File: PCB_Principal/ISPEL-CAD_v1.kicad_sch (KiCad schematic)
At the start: 21 parts, among them J1 Vin, J10 E1, J11 S1, J12 E2, J13 S2, J14 FRENTE, J15 PRUEBA_5V, J2 GND_NUCLEO, J3 CN8_NUCLEO, J4 CN9_NUCLEO, J5 GND_NUCLEO, J6 GND_NUCLEO, J7 CN7_NUCLEO, J8 CN10_NUCLEO, J9 GND_NUCLEO

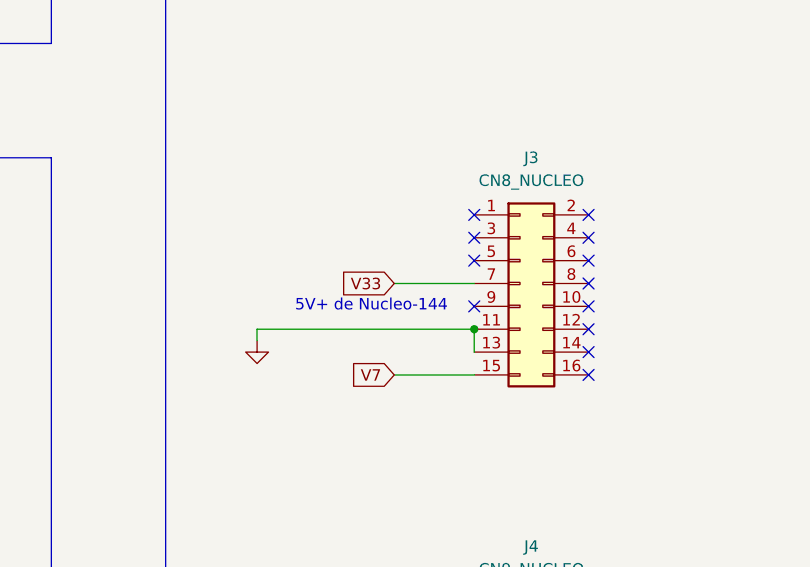
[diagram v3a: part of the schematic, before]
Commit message: Placa PCB con ERC. Falta huella de portafusibles.
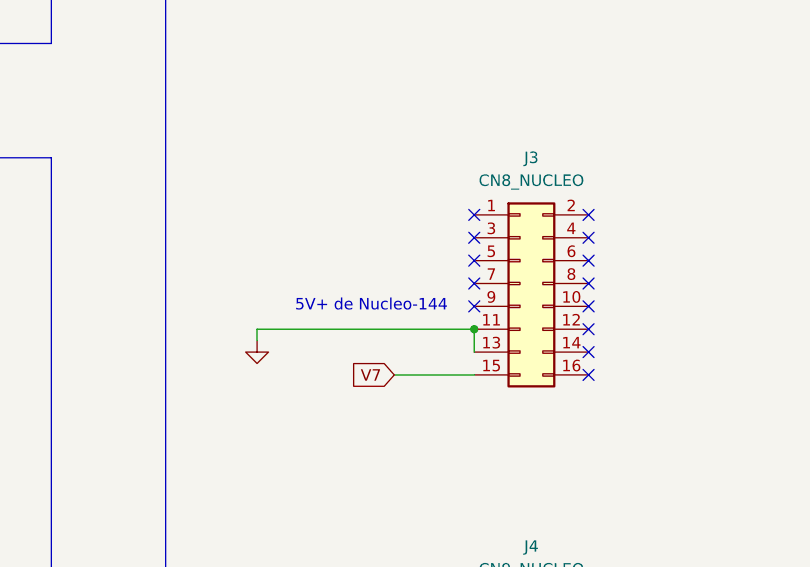
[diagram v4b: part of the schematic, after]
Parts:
- J3: footprint Connector_PinSocket_2.54mm:PinSocket_2x08_P2.54mm_Vertical -> Libreria_ISPEL:PinSocket_2x08_P2.54mm_Vertical_impar-par
- J4: footprint Connector_PinSocket_2.54mm:PinSocket_2x16_P2.54mm_Vertical -> Libreria_ISPEL:PinSocket_2x16_P2.54mm_Vertical_impar-par
- J7: footprint Connector_PinSocket_2.54mm:PinSocket_2x10_P2.54mm_Vertical -> Libreria_ISPEL:PinSocket_2x10_P2.54mm_Vertical_impar-par
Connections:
- net V33: no longer names the net of J3.7 (Pin_7)
- no-connect marks 61 -> 62
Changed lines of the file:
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@@
 	)
 	(no_connect
+		(at 110.49 153.67)
+	)
+	(no_connect
 		(at 186.69 163.83)
 	)
@@
 	(wire
 		(pts
-			(xy 101.6 153.67) (xy 110.49 153.67)
-		)
-		(stroke
-			(width 0)
-			(type default)
-		)
-	)
-	(wire
-		(pts
 			(xy 290.83 186.69) (xy 284.48 186.69)
 		)
@@
 		)
 	)
-	(global_label "V33"
-		(shape input)
-		(at 101.6 153.67 180)
-		(fields_autoplaced yes)
-		(effects
-			(font
-				(size 1.27 1.27)
-			)
-			(justify right)
-		)
-		(property "Intersheetrefs" "${INTERSHEET_REFS}"
-			(at 95.1072 153.67 0)
-			(effects
-				(font
-					(size 1.27 1.27)
-				)
-				(justify right)
-				(hide yes)
-			)
-		)
-	)
 	(global_label "ADC1_C20"
 		(shape input)
@@
 			)
 		)
-		(property "Footprint" "Connector_PinSocket_2.54mm:PinSocket_2x10_P2.54mm_Vertical"
+		(property "Footprint" "Libreria_ISPEL:PinSocket_2x10_P2.54mm_Vertical_impar-par"
 			(at 179.07 151.13 0)
 			(effects
@@
 			)
 		)
-		(property "Footprint" "Connector_PinSocket_2.54mm:PinSocket_2x16_P2.54mm_Vertical"
+		(property "Footprint" "Libreria_ISPEL:PinSocket_2x16_P2.54mm_Vertical_impar-par"
 			(at 115.57 207.01 0)
 			(effects
@@
 			)
 		)
-		(property "Footprint" "Connector_PinSocket_2.54mm:PinSocket_2x08_P2.54mm_Vertical"
+		(property "Footprint" "Libreria_ISPEL:PinSocket_2x08_P2.54mm_Vertical_impar-par"
 			(at 115.57 153.67 0)
 			(effects

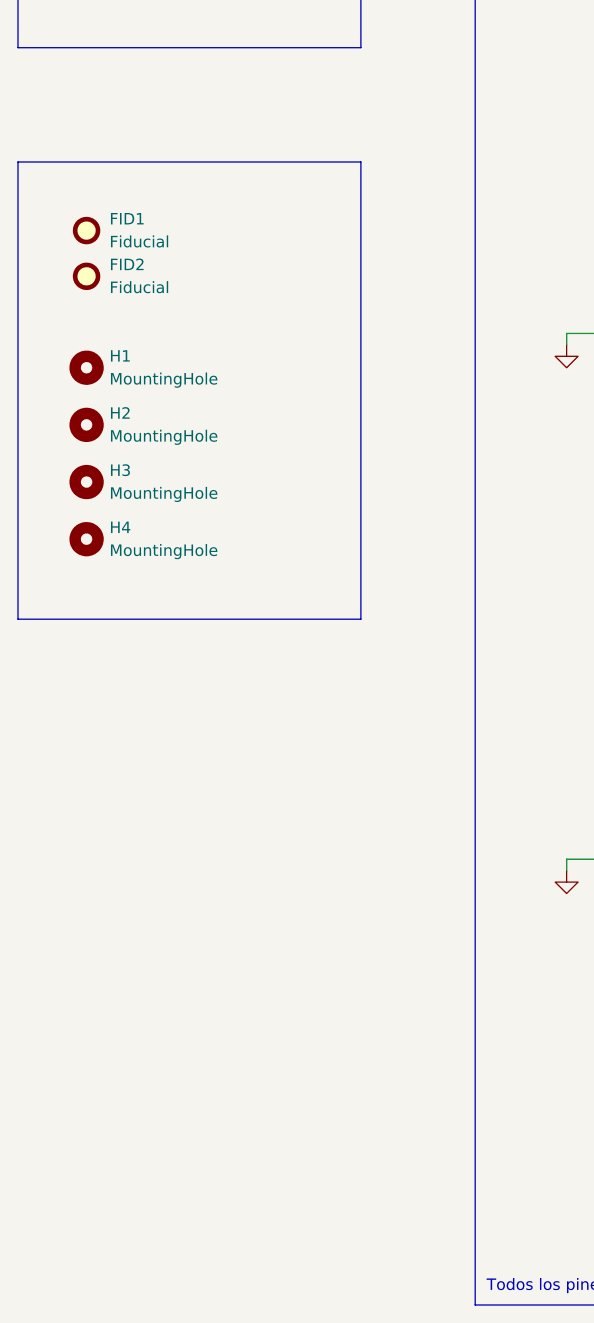
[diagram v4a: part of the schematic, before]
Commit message: PCB con huella de portafusibles 1808.
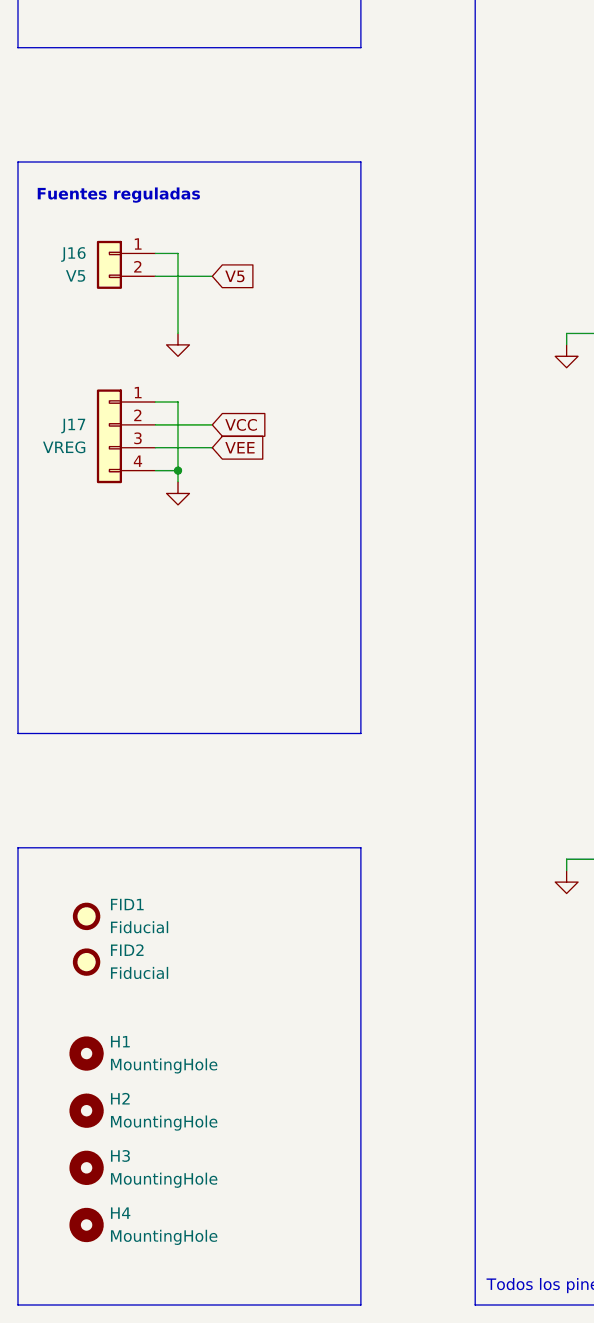
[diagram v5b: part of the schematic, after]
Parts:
- added J16: V5, Connector_PinSocket_2.54mm:PinSocket_1x02_P2.54mm_Vertical, symbol Connector_Generic:Conn_01x02
- added J17: VREG, Connector_PinSocket_2.54mm:PinSocket_1x04_P2.54mm_Vertical, symbol Connector_Generic:Conn_01x04
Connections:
- net GND: now also J16.1 (Pin_1), J17.1 (Pin_1), J17.4 (Pin_4)
- net V5: now also J16.2 (Pin_2)
- new net VCC: J17.2 (Pin_2)
- new net VEE: J17.3 (Pin_3)
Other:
- note added: "Fuentes reguladas"
- moved on the sheet: FID1, FID2, H1, H2, H3, H4

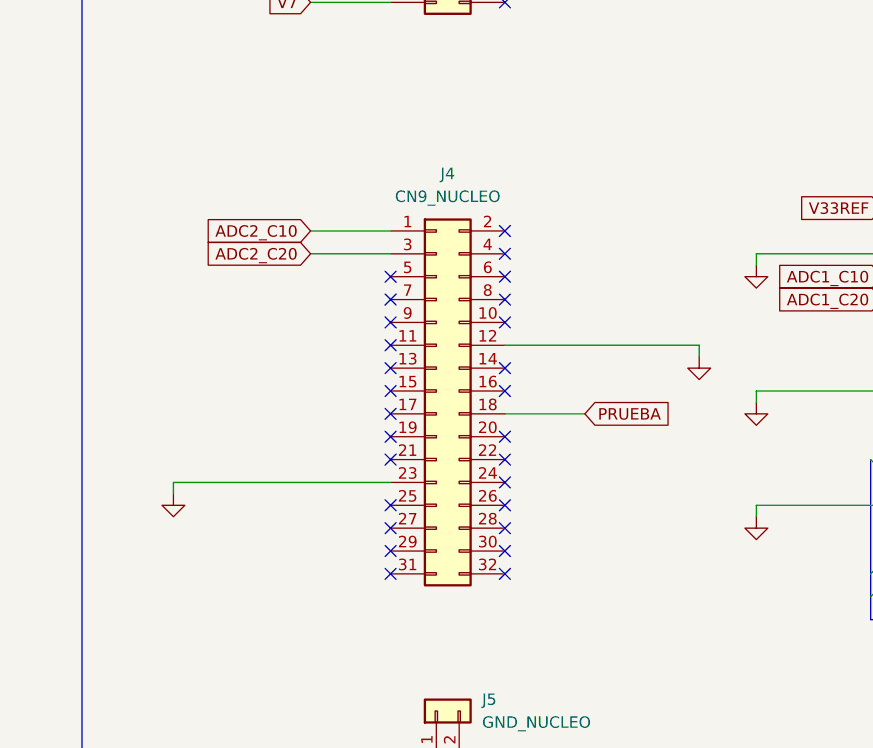
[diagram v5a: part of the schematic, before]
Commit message: Corrección de conector.
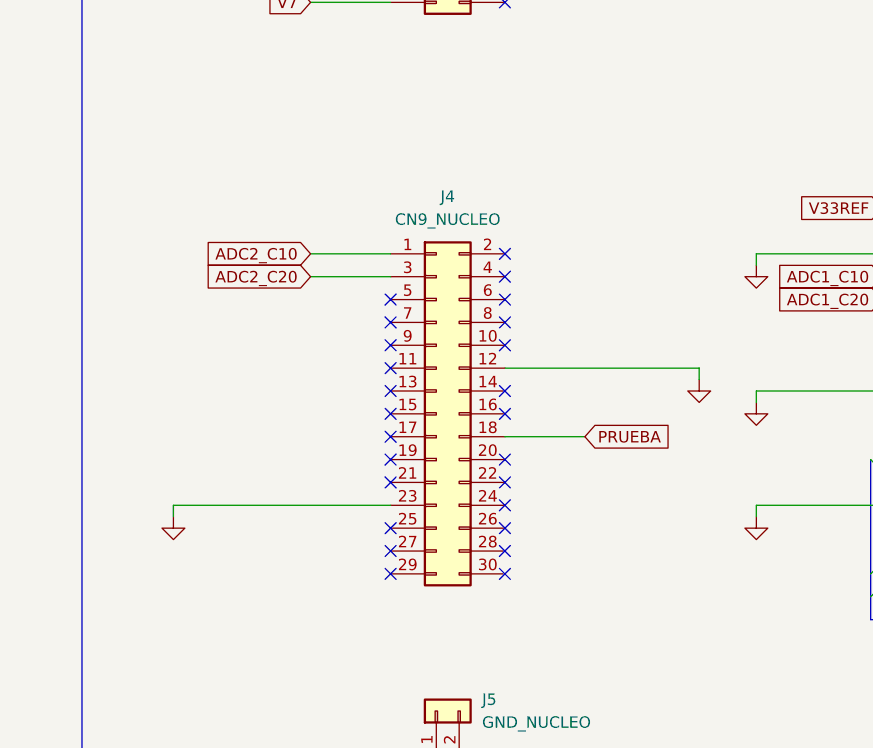
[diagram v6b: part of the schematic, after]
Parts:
- removed J4: CN9_NUCLEO, Libreria_ISPEL:PinSocket_2x16_P2.54mm_Vertical_impar-par, symbol Connector_Generic:Conn_02x16_Odd_Even
- added J4: CN9_NUCLEO, Libreria_ISPEL:PinSocket_2x15_P2.54mm_Vertical_impar-par, symbol Connector_Generic:Conn_02x15_Odd_Even
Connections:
- net ADC2_C10: now also J4.1 (Pin_1)
- net ADC2_C20: now also J4.3 (Pin_3)
- net GND: now also J4.12 (Pin_12), J4.23 (Pin_23)
- net PRUEBA: now also J4.18 (Pin_18)
- no-connect marks 62 -> 60

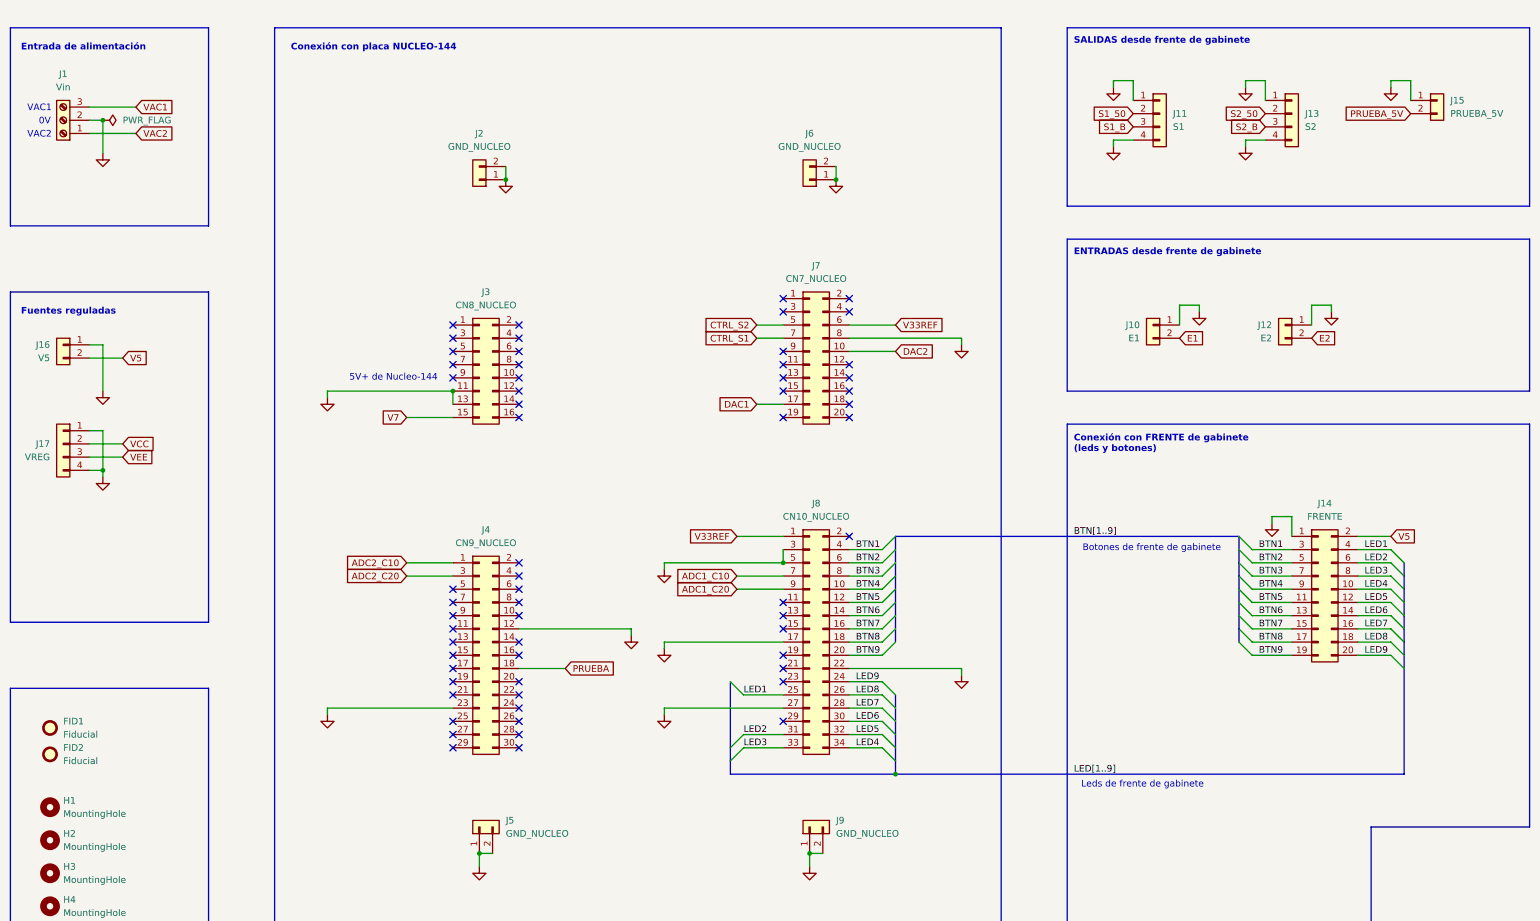
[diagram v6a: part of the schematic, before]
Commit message: Agregado de leyendas y pin para sensor de temperatura.
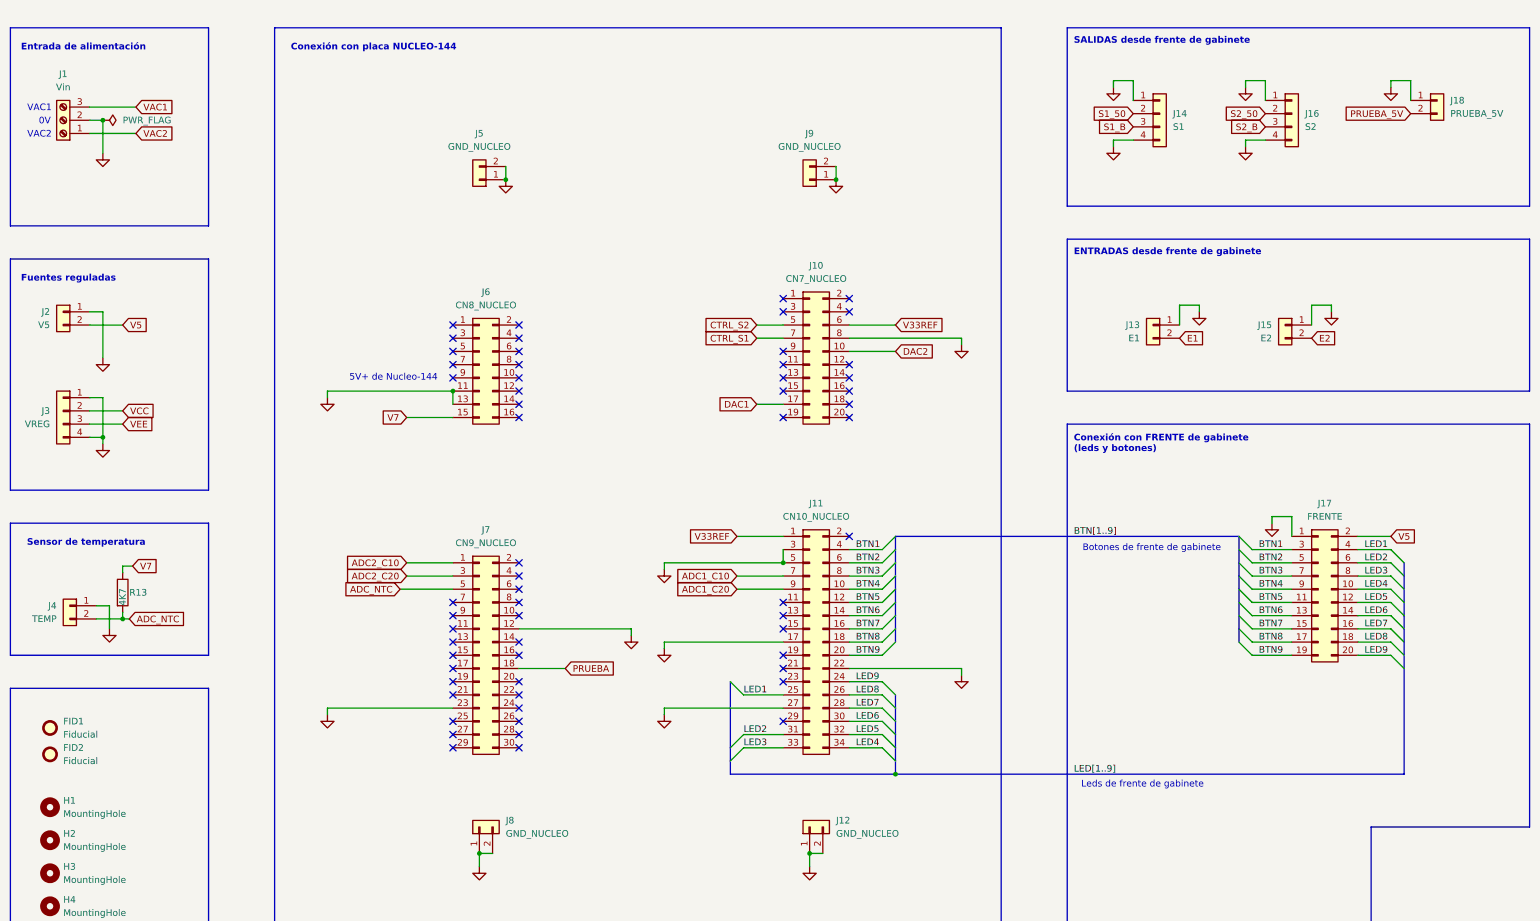
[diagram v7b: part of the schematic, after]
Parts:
- added J4: TEMP, Connector_PinHeader_2.54mm:PinHeader_1x02_P2.54mm_Vertical, symbol Connector_Generic:Conn_01x02
- added R13: 4K7, Resistor_SMD:R_1206_3216Metric_Pad1.30x1.75mm_HandSolder, symbol Device:R
- renumbered J7 to J10, J8 to J11, J9 to J12, J10 to J13, J11 to J14, J12 to J15, J13 to J16, J14 to J17, J15 to J18, J16 to J2, J17 to J3, J2 to J5, J3 to J6, J4 to J7, J5 to J8, J6 to J9
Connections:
- net GND: now also J4.1 (Pin_1)
- net V7: now also R13.1
- net ADC_NTC: now reaches J7.5 (Pin_5)
- net ADC_NTC: now also J4.2 (Pin_2), R13.2
- no-connect marks 60 -> 59
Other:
- note added: "Sensor de temperatura"
- moved on the sheet: J2, J3

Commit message: Corrigiendo anotaciones.
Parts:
- added H5: MountingHole, MountingHole:MountingHole_3.2mm_M3, symbol Mechanical:MountingHole
- added R14: 0, Resistor_SMD:R_1206_3216Metric_Pad1.30x1.75mm_HandSolder, symbol Device:R
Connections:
- net V5: now also R13.1
- net V7: now also R14.1; no longer J6.15 (Pin_15), R13.1
- new net: J6.15 (Pin_15), R14.2
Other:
- moved on the sheet: H1, H2, H3, H4, J4, R13
